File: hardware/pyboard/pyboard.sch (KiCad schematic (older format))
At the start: 65 parts, among them J1 Battery, J2 Arduino_Mega2560_Shield, J6 USB_B_Micro, J9 Micro_SD_SCHA5B0200, Q1 IRLML6402, Q2 IRLML6402, SW1 RST, SW2 USR, U1 STM32F405RGT6, U2 MCP1703A-3302_SOT89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

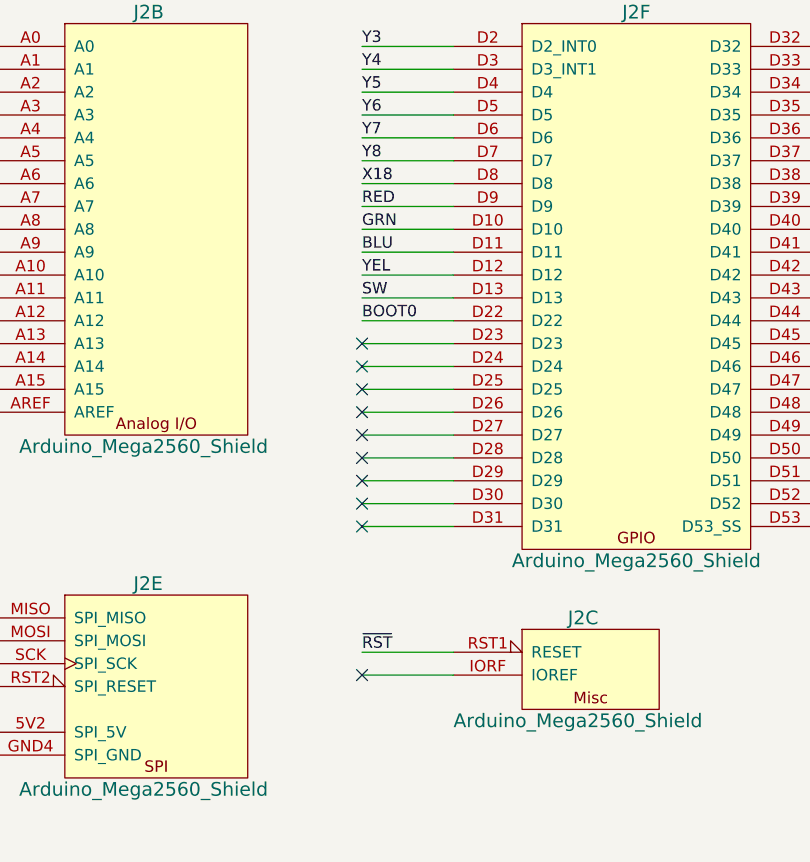
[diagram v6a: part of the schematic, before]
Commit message: Change X18 pin binding
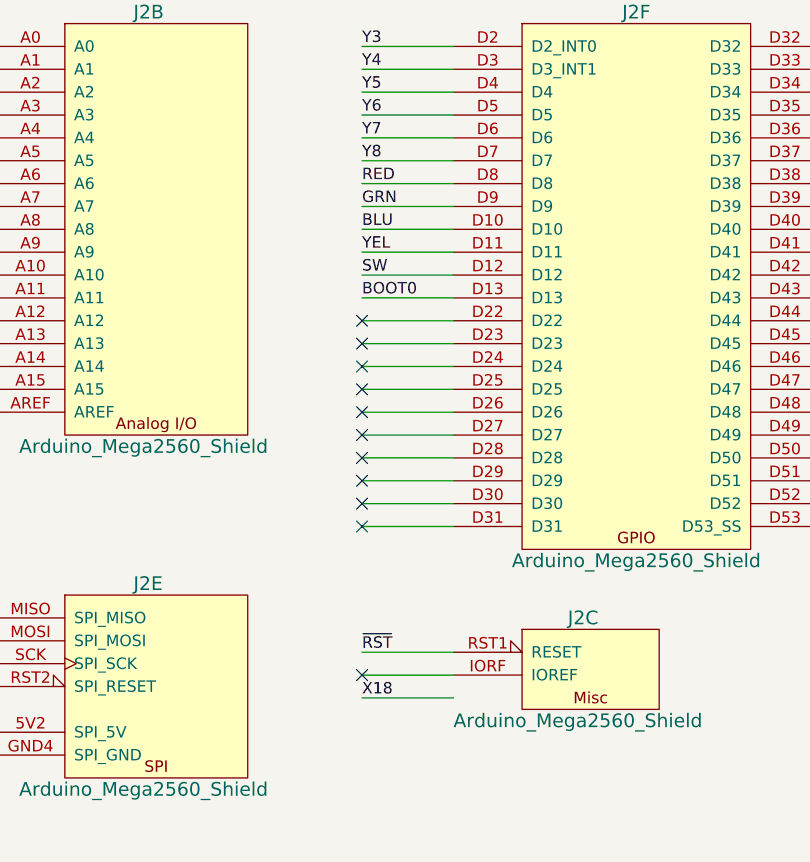
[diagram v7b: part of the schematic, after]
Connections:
- wire segments 375 -> 376
- no-connect marks 45 -> 46
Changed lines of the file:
@@
 Text Label 17450 5050 0    50   ~ 0
 X12
-Text Label 19450 5550 0    50   ~ 0
-BOOT0
-Text Label 19450 5450 0    50   ~ 0
+Text Label 19450 5350 0    50   ~ 0
 SW
 Text Label 17450 5250 0    50   ~ 0
@@
 Text Label 17450 5150 0    50   ~ 0
 X19
-Text Label 19450 4950 0    50   ~ 0
-X18
 Wire Wire Line
 	19850 5950 19450 5950
 Wire Wire Line
+	19850 5150 19450 5150
+Wire Wire Line
+	19850 4850 19450 4850
+Wire Wire Line
+	19850 4750 19450 4750
+Wire Wire Line
+	19850 4650 19450 4650
+Wire Wire Line
+	19850 4550 19450 4550
+Wire Wire Line
+	19850 5850 19450 5850
+Wire Wire Line
+	19850 5650 19450 5650
+Wire Wire Line
+	19850 5350 19450 5350
+Wire Wire Line
 	19850 5250 19450 5250
 Wire Wire Line
+	19850 4450 19450 4450
+Wire Wire Line
+	19850 4350 19450 4350
+Wire Wire Line
 	19850 4950 19450 4950
-Wire Wire Line
-	19850 4850 19450 4850
-Wire Wire Line
-	19850 4750 19450 4750
-Wire Wire Line
-	19850 4650 19450 4650
-Wire Wire Line
-	19850 4550 19450 4550
-Wire Wire Line
-	19850 5850 19450 5850
-Wire Wire Line
-	19850 5650 19450 5650
-Wire Wire Line
-	19850 5550 19450 5550
-Wire Wire Line
-	19850 5450 19450 5450
-Wire Wire Line
-	19850 5350 19450 5350
-Wire Wire Line
-	19850 4450 19450 4450
-Wire Wire Line
-	19850 4350 19450 4350
-Wire Wire Line
-	19850 5050 19450 5050
 Wire Wire Line
 	21850 5950 21450 5950
@@
 Wire Wire Line
 	21850 6050 21450 6050
+Text Label 19450 5150 0    50   ~ 0
+BLU
 Text Label 19450 5250 0    50   ~ 0
-BLU
-Text Label 19450 5350 0    50   ~ 0
 YEL
-Text Label 19450 5150 0    50   ~ 0
+Text Label 19450 5050 0    50   ~ 0
 GRN
-Text Label 19450 5050 0    50   ~ 0
+Text Label 19450 4950 0    50   ~ 0
 RED
 Wire Wire Line
-	19850 5150 19450 5150
+	19850 5050 19450 5050
 Wire Wire Line
 	17850 7150 17450 7150
@@
 NoConn ~ 15450 4750
 NoConn ~ 15450 4850
+Text Label 19450 7200 0    50   ~ 0
+X18
+Wire Wire Line
+	19850 7200 19450 7200
+Text Label 19450 5450 0    50   ~ 0
+BOOT0
+Wire Wire Line
+	19850 5450 19450 5450
+Wire Wire Line
+	19850 5550 19450 5550
+NoConn ~ 19450 5550
 $EndSCHEMATC

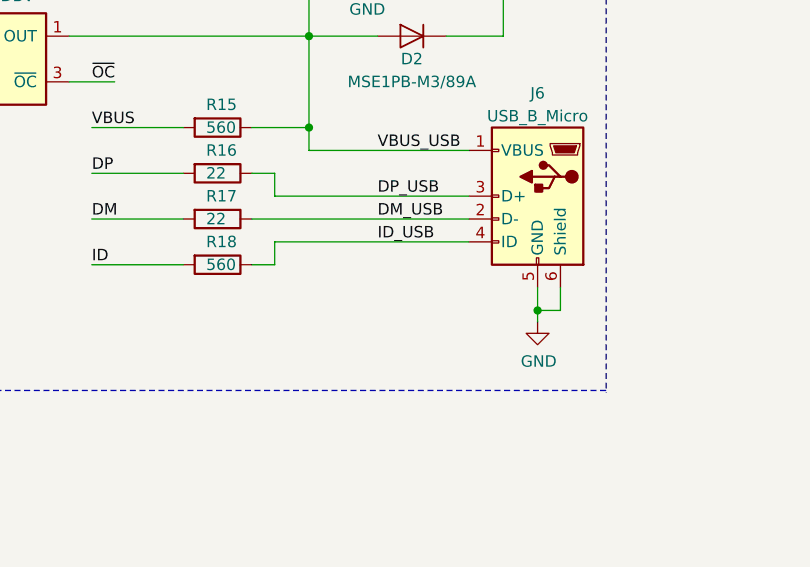
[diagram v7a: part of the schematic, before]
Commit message: Configure track width
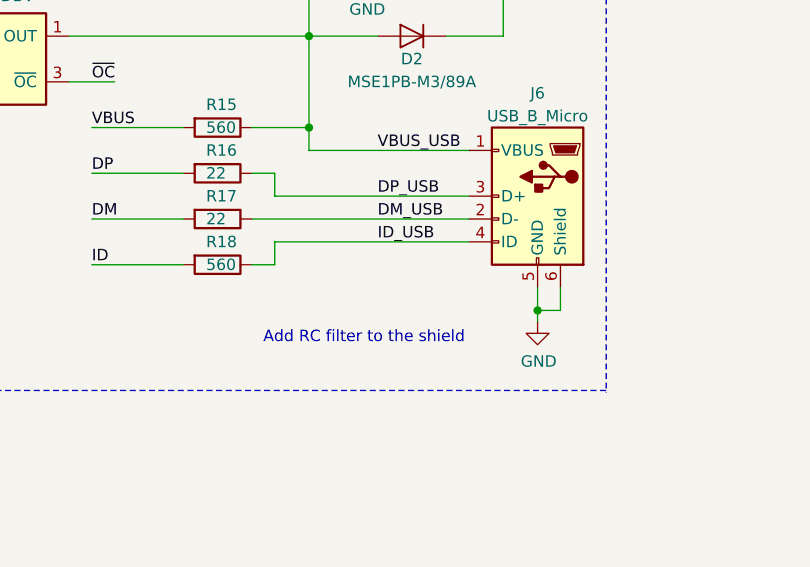
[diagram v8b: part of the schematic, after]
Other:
- note added: "Add RC filter to the shield\n"
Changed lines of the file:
@@
 	11400 3450 11400 3550
 Wire Wire Line
-	12250 3450 11400 3450
-Wire Wire Line
 	11400 3150 11300 3150
 Wire Wire Line
 	11400 3250 11400 3150
-Wire Wire Line
-	12250 3250 11400 3250
-Wire Wire Line
-	12250 3350 11300 3350
 Wire Wire Line
 	10600 2950 11000 2950
@@
 	19850 5550 19450 5550
 NoConn ~ 19450 5550
+Wire Wire Line
+	12250 3250 11400 3250
+Wire Wire Line
+	11300 3350 12250 3350
+Wire Wire Line
+	12250 3450 11400 3450
+Text Notes 11350 3900 0    50   ~ 0
+Add RC filter to the shield\n
 $EndSCHEMATC
